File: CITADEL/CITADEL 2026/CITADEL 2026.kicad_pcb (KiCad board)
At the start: 2 copper layers, 141.5 x 109.7 mm, 61 parts, among them Q7 SSM3K329R_LF, U1 PCA9685PW_118, U3 TJA1051T-3, U4 ESP32-S3-DEVKITC-1-N8R8

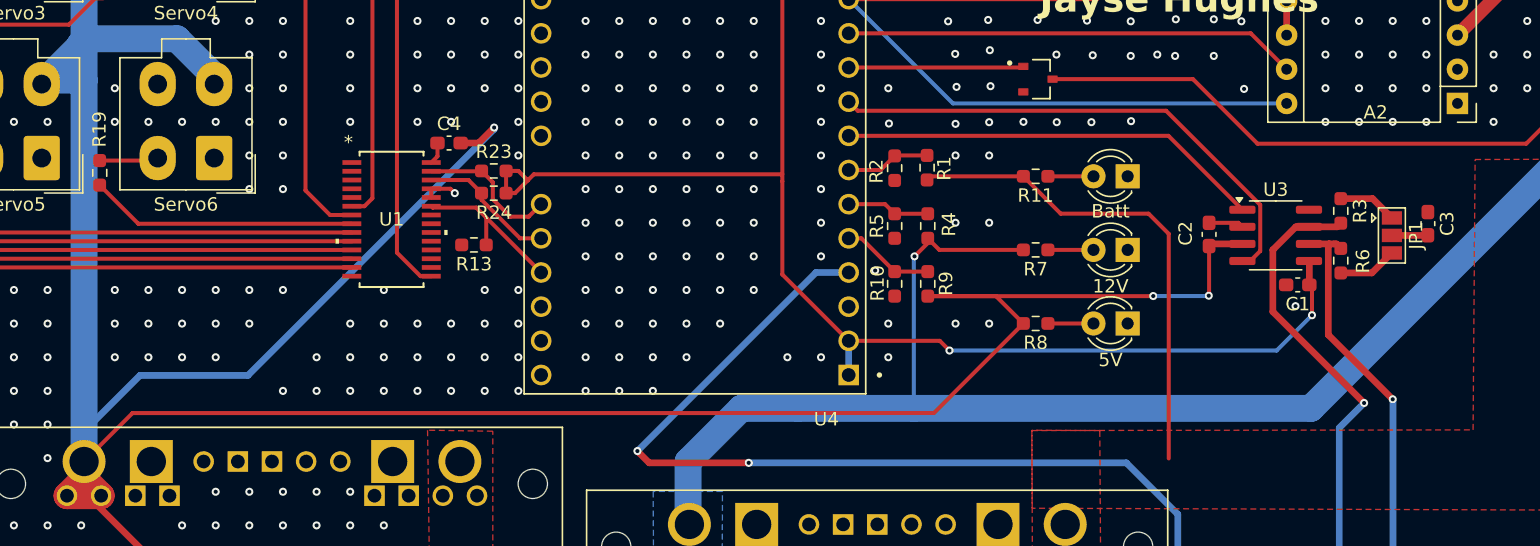
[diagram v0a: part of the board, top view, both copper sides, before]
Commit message: Changed 5V trace for PCA9685
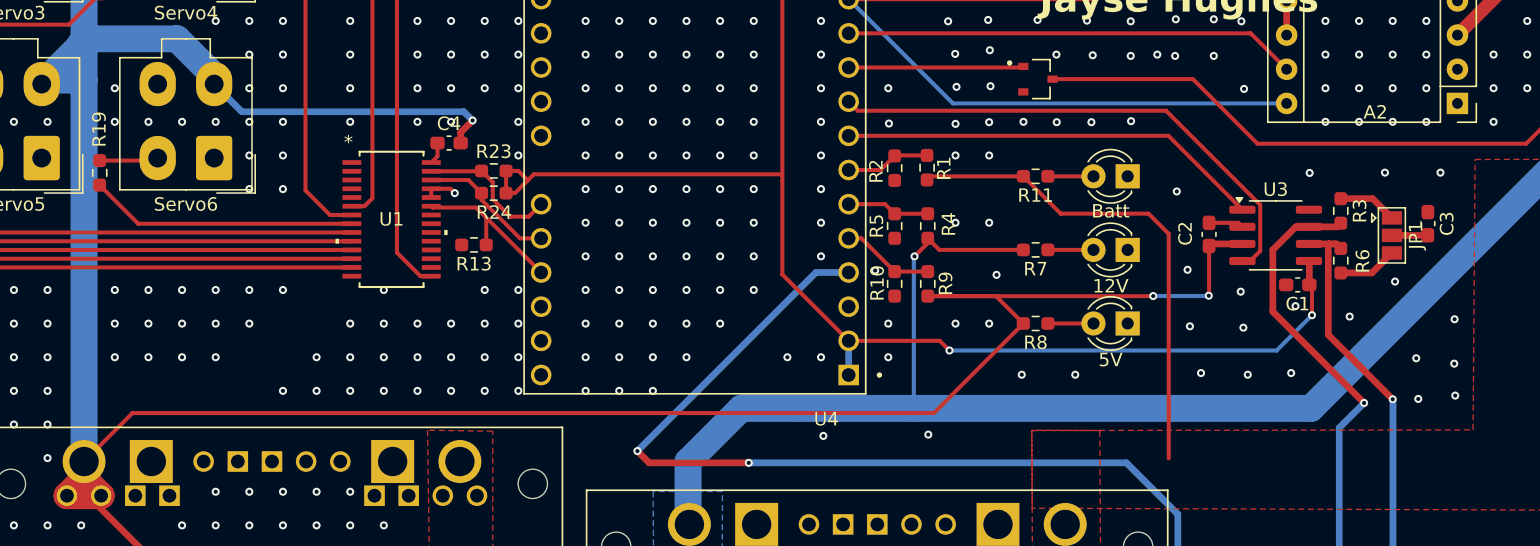
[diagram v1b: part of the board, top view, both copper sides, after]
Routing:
- net +5V: track 494.9 -> 472.1 mm
- net GND: vias 988 -> 1011
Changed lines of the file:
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@@
 	)
 	(segment
+		(start 59.7625 70.275)
+		(end 59.7625 69.4875)
+		(width 0.5)
+		(layer "F.Cu")
+		(net 3)
+	)
+	(segment
 		(start 121.67 107.035)
 		(end 118.775 109.93)
@@
 	)
 	(segment
-		(start 35.3675 90.35)
-		(end 31.765 93.9525)
-		(width 0.3)
+		(start 59.7625 69.4875)
+		(end 60.65 68.6)
+		(width 0.5)
 		(layer "F.Cu")
 		(net 3)
 	)
 	(segment
-		(start 61.1 70.275)
-		(end 62.25 69.125)
-		(width 0.5)
+		(start 35.3675 90.35)
+		(end 31.765 93.9525)
+		(width 0.3)
 		(layer "F.Cu")
 		(net 3)
@@
 	)
 	(segment
-		(start 59.7625 70.275)
-		(end 61.1 70.275)
-		(width 0.5)
-		(layer "F.Cu")
-		(net 3)
-	)
-	(segment
 		(start 118.775 113.8125)
 		(end 116.8875 115.7)
@@
 	)
 	(via
-		(at 62.25 69.125)
+		(at 60.65 68.6)
 		(size 0.6)
 		(drill 0.3)
@@
 	)
 	(segment
-		(start 31.775 93.9525)
-		(end 31.765 93.9525)
-		(width 0.5)
-		(layer "B.Cu")
-		(net 3)
-	)
-	(segment
 		(start 39.275 33.725)
 		(end 41.437 35.887)
@@
 	)
 	(segment
-		(start 31.775 91.7)
-		(end 31.775 93.9525)
-		(width 0.5)
-		(layer "B.Cu")
-		(net 3)
-	)
-	(segment
 		(start 28.617 37.452)
 		(end 32.344 33.725)
@@
 	)
 	(segment
-		(start 62.25 69.125)
-		(end 62.25 69.25)
+		(start 59.999 67.949)
+		(end 43.494 67.949)
 		(width 0.5)
 		(layer "B.Cu")
@@
 	)
 	(segment
-		(start 62.25 69.25)
-		(end 43.95 87.55)
-		(width 0.5)
+		(start 31.765 93.9525)
+		(end 31.765 65.6)
+		(width 2)
 		(layer "B.Cu")
 		(net 3)
 	)
 	(segment
-		(start 31.765 93.9525)
-		(end 31.765 65.6)
-		(width 2)
+		(start 60.65 68.6)
+		(end 59.999 67.949)
+		(width 0.5)
 		(layer "B.Cu")
 		(net 3)
@@
 	)
 	(segment
-		(start 43.95 87.55)
-		(end 35.925 87.55)
+		(start 43.494 67.949)
+		(end 41.437 65.892)
 		(width 0.5)
 		(layer "B.Cu")
@@
 	)
 	(segment
-		(start 35.925 87.55)
-		(end 31.775 91.7)
-		(width 0.5)
-		(layer "B.Cu")
-		(net 3)
-	)
-	(segment
 		(start 31.9 62.525)
 		(end 38.675 62.525)
@@
 	)
 	(via
+		(at 128.475 72.475)
+		(size 0.6)
+		(drill 0.3)
+		(layers "F.Cu" "B.Cu")
+		(free yes)
+		(net 11)
+	)
+	(via
 		(at 61.55 56.2)
 		(size 0.6)
@@
 	)
 	(via
+		(at 130.8 86.275)
+		(size 0.6)
+		(drill 0.3)
+		(layers "F.Cu" "B.Cu")
+		(free yes)
+		(net 11)
+	)
+	(via
 		(at 109.575 63.8)
 		(size 0.6)
@@
 	)
 	(via
+		(at 122.875 72.5)
+		(size 0.6)
+		(drill 0.3)
+		(layers "F.Cu" "B.Cu")
+		(free yes)
+		(net 11)
+	)
+	(via
 		(at 56.55 83.7)
 		(size 0.6)
@@
 	)
 	(via
+		(at 133.65 83.375)
+		(size 0.6)
+		(drill 0.3)
+		(layers "F.Cu" "B.Cu")
+		(free yes)
+		(net 11)
+	)
+	(via
 		(at 21.55 68.7)
 		(size 0.6)
@@
 	)
 	(via
+		(at 121.5 87.375)
+		(size 0.6)
+		(drill 0.3)
+		(layers "F.Cu" "B.Cu")
+		(free yes)
+		(net 11)
+	)
+	(via
 		(at 81.55 56.2)
 		(size 0.6)
@@
 	)
 	(via
+		(at 94.525 91.95)
+		(size 0.6)
+		(drill 0.3)
+		(layers "F.Cu" "B.Cu")
+		(free yes)
+		(net 11)
+	)
+	(via
 		(at 46.55 58.7)
 		(size 0.6)
@@
 	)
 	(via
+		(at 118.275 87.5)
+		(size 0.6)
+		(drill 0.3)
+		(layers "F.Cu" "B.Cu")
+		(free yes)
+		(net 11)
+	)
+	(via
 		(at 39.05 128.7)
 		(size 0.6)
@@
 	)
 	(via
+		(at 113.975 83.9)
+		(size 0.6)
+		(drill 0.3)
+		(layers "F.Cu" "B.Cu")
+		(free yes)
+		(net 11)
+	)
+	(via
 		(at 64.05 83.7)
 		(size 0.6)
@@
 	)
 	(via
+		(at 133.7 89.05)
+		(size 0.6)
+		(drill 0.3)
+		(layers "F.Cu" "B.Cu")
+		(free yes)
+		(net 11)
+	)
+	(via
 		(at 56.55 128.7)
 		(size 0.6)
@@
 	)
 	(via
+		(at 117.75 81.325)
+		(size 0.6)
+		(drill 0.3)
+		(layers "F.Cu" "B.Cu")
+		(free yes)
+		(net 11)
+	)
+	(via
 		(at 41.55 126.2)
 		(size 0.6)
@@
 	)
 	(via
+		(at 129.225 80.575)
+		(size 0.6)
+		(drill 0.3)
+		(layers "F.Cu" "B.Cu")
+		(free yes)
+		(net 11)
+	)
+	(via
 		(at 46.55 128.7)
 		(size 0.6)
@@
 	)
 	(via
+		(at 132.6 72.475)
+		(size 0.6)
+		(drill 0.3)
+		(layers "F.Cu" "B.Cu")
+		(free yes)
+		(net 11)
+	)
+	(via
 		(at 16.55 38.7)
 		(size 0.6)
@@
 	)
 	(via
+		(at 86.725 92.05)
+		(size 0.6)
+		(drill 0.3)
+		(layers "F.Cu" "B.Cu")
+		(free yes)
+		(net 11)
+	)
+	(via
 		(at 81.55 121.2)
 		(size 0.6)
@@
 	)
 	(via
+		(at 130.95 89.3)
+		(size 0.6)
+		(drill 0.3)
+		(layers "F.Cu" "B.Cu")
+		(free yes)
+		(net 11)
+	)
+	(via
 		(at 96.55 33.7)
 		(size 0.6)
@@
 	)
 	(via
+		(at 125.85 83.175)
+		(size 0.6)
+		(drill 0.3)
+		(layers "F.Cu" "B.Cu")
+		(free yes)
+		(net 11)
+	)
+	(via
 		(at 29.05 28.7)
 		(size 0.6)
@@
 	)
 	(via
+		(at 133.625 86.675)
+		(size 0.6)
+		(drill 0.3)
+		(layers "F.Cu" "B.Cu")
+		(free yes)
+		(net 11)
+	)
+	(via
 		(at 118 66.25)
 		(size 0.6)
@@
 	)
 	(via
+		(at 99.6 80.075)
+		(size 0.6)
+		(drill 0.3)
+		(layers "F.Cu" "B.Cu")
+		(free yes)
+		(net 11)
+	)
+	(via
 		(at 44.05 103.7)
 		(size 0.6)
@@
 	)
 	(via
+		(at 113 73.875)
+		(size 0.6)
+		(drill 0.3)
+		(layers "F.Cu" "B.Cu")
+		(free yes)
+		(net 11)
+	)
+	(via
 		(at 151.55 113.7)
 		(size 0.6)
@@
 	)
 	(via
+		(at 117.95 84)
+		(size 0.6)
+		(drill 0.3)
+		(layers "F.Cu" "B.Cu")
+		(free yes)
+		(net 11)
+	)
+	(via
 		(at 29.05 128.7)
 		(size 0.6)
@@
 	)
 	(via
+		(at 101.475 87.5)
+		(size 0.6)
+		(drill 0.3)
+		(layers "F.Cu" "B.Cu")
+		(free yes)
+		(net 11)
+	)
+	(via
 		(at 41.55 28.7)
 		(size 0.6)
@@
 	)
 	(via
+		(at 105.45 87.5)
+		(size 0.6)
+		(drill 0.3)
+		(layers "F.Cu" "B.Cu")
+		(free yes)
+		(net 11)
+	)
+	(via
+		(at 113.8 79.7)
+		(size 0.6)
+		(drill 0.3)
+		(layers "F.Cu" "B.Cu")
+		(free yes)
+		(net 11)
+	)
+	(via
 		(at 118.175 38.8)
 		(size 0.6)
@@
 		(net 11)
 	)
+	(via
+		(at 114.8 87.375)
+		(size 0.6)
+		(drill 0.3)
+		(layers "F.Cu" "B.Cu")
+		(free yes)
+		(net 11)
+	)
